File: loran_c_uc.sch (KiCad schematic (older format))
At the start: 33 parts, among them U1 STM32F407VG

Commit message: Almost done: SPI, Relay optocouplers, ADC & DAC interface However, bug needs to be fixed: buses are not connected between hierarchical sheets
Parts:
- removed C7, C8: 2.2u 6.3v, symbol CP1
- removed D? (x2): SMLVT3V3, symbol ZENER
- added C701: 10n, symbol C
- added C712, C713: 2.2u 10V CER, symbol C
- added D701: BAS85, symbol DIODESCH
- added JP702: RESET, symbol JUMPER
- added R709, R710: 33, symbol R
- C704, C705: renamed from C?; value 2.2u TAN -> 10u 6.3V Ta
- C711: renamed from C6; value 4.7u 6.3v -> 10u 6.3V Ta
- gave numbers to parts that had none: 20
- renumbered C1 to C706, C2 to C707, C3 to C708, C4 to C709, C5 to C710, U1 to U701
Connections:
- net labels added: BPROG, BREL, BSWD, NTRST, REL1, REL2, REL3, REL4, RELAY, SPI_STRB, SWCLK, SWD, SWDIO
- net labels removed: BJTAG, BPROGOUT, JTAG_SWD, JTAG_TCK_SWCLK, JTAG_TDI, JTAG_TMS_SWDIO, SPI_RD, SPI_WR
- wire segments 139 -> 125
- no-connect marks 0 -> 35
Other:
- moved on the sheet: JP701, R704

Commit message: FIXED: no more buses on hierarchical sheet ports
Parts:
- added R715: 33, symbol R
- FB701: value BEAD -> Bead
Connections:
- net SWDIO: now also R715.1; no longer U701.72 (PA13/JTMS/SWDIO/EVENTOUT)
- net NTRST renamed SWNTRST
- net REL1 renamed RELAY1
- net REL2 renamed RELAY2
- net REL3 renamed RELAY3
- net REL4 renamed RELAY4
- new net: R715.2, U701.72 (PA13/JTMS/SWDIO/EVENTOUT)
- no-connect marks 35 -> 39
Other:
- moved on the sheet: C714, C715, D701, X701

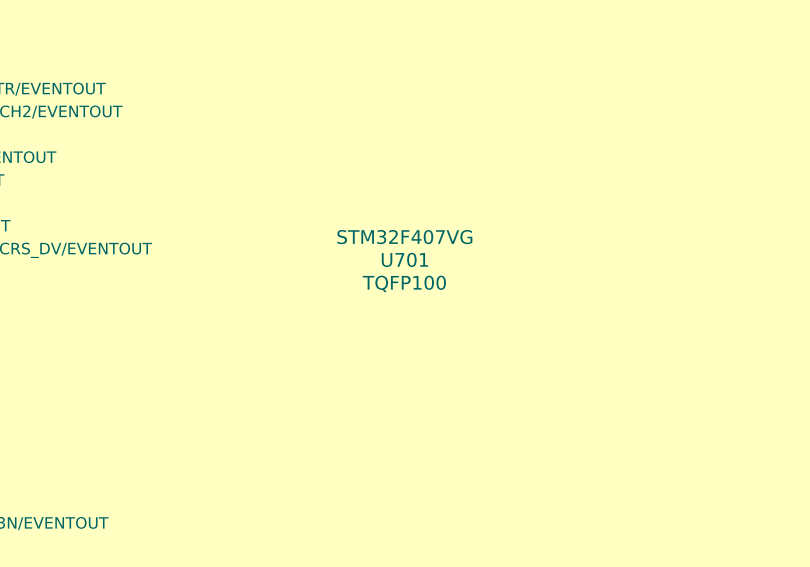
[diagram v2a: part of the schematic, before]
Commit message: Update: fix, assign modules to components -Fix P302 incorrect connection -Assign footprints to components (not all yet) -Back-import footprints into schematic fields
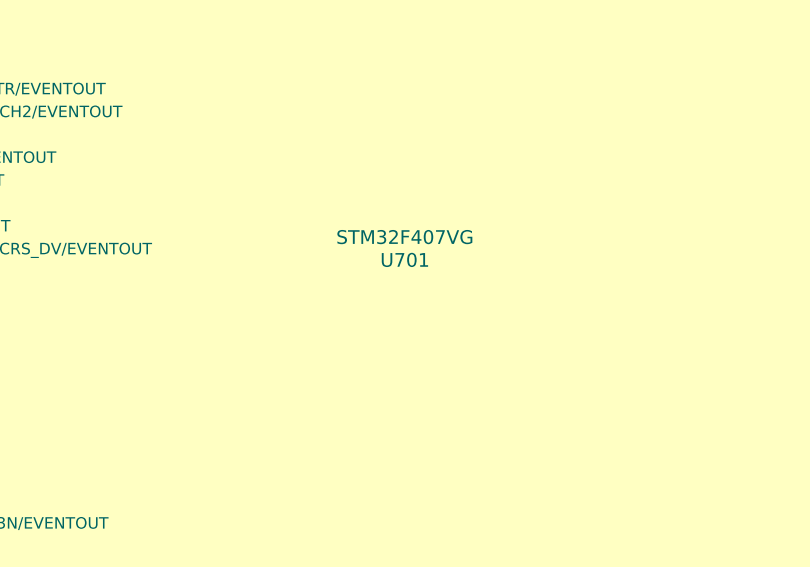
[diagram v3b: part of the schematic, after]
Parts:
- C701, C702, C703, C706, C707, C708, C709, C710, C712, C713, C714, C715: footprint (none) -> w_smd_capacitors:c_1206
- C704, C705, C711: footprint (none) -> w_smd_capacitors:c_tant_B
- D701, D702: footprint (none) -> w_smd_diode:sod80c
- FB701: footprint (none) -> w_pth_resistors:RC07
- JP701, JP702: footprint (none) -> Pin_Headers:Pin_Header_Straight_1x02
- R701, R702, R703, R704, R705, R706, R707, R708, R709, R710, R711, R712, R713, R714, R715: footprint (none) -> w_smd_resistors:r_1206
- U701: footprint TQFP100 -> w_smd_lqfp:TQFP-100
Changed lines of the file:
@@
 Date "15 янв. 2014"
 Rev "1"
-Comp "Roman Dobrodiy"
+Comp "Roman Dobrodiy (aka RomaVis)"
 Comment1 ""
 Comment2 ""
@@
 F 0 "U701" H 8350 5250 60  0000 C CNN
 F 1 "STM32F407VG" H 8350 5350 60  0000 C CNN
-F 2 "TQFP100" H 8350 5150 60  0000 C CNN
+F 2 "w_smd_lqfp:TQFP-100" H 8350 5150 60  0001 C CNN
 F 3 "" H 8350 5250 60  0000 C CNN
 	1    8350 5250
@@
 F 0 "C706" H 7600 1500 40  0000 L CNN
 F 1 "100n" H 7606 1315 40  0000 L CNN
-F 2 "" H 7638 1250 30  0000 C CNN
+F 2 "w_smd_capacitors:c_1206" H 7638 1250 30  0001 C CNN
 F 3 "" H 7600 1400 60  0000 C CNN
 	1    7600 1400
@@
 F 0 "C707" H 7900 1500 40  0000 L CNN
 F 1 "100n" H 7906 1315 40  0000 L CNN
-F 2 "" H 7938 1250 30  0000 C CNN
+F 2 "w_smd_capacitors:c_1206" H 7938 1250 30  0001 C CNN
 F 3 "" H 7900 1400 60  0000 C CNN
 	1    7900 1400
@@
 F 0 "C708" H 8200 1500 40  0000 L CNN
 F 1 "100n" H 8206 1315 40  0000 L CNN
-F 2 "" H 8238 1250 30  0000 C CNN
+F 2 "w_smd_capacitors:c_1206" H 8238 1250 30  0001 C CNN
 F 3 "" H 8200 1400 60  0000 C CNN
 	1    8200 1400
@@
 F 0 "C709" H 8500 1500 40  0000 L CNN
 F 1 "100n" H 8506 1315 40  0000 L CNN
-F 2 "" H 8538 1250 30  0000 C CNN
+F 2 "w_smd_capacitors:c_1206" H 8538 1250 30  0001 C CNN
 F 3 "" H 8500 1400 60  0000 C CNN
 	1    8500 1400
@@
 F 0 "C710" H 8800 1500 40  0000 L CNN
 F 1 "100n" H 8806 1315 40  0000 L CNN
-F 2 "" H 8838 1250 30  0000 C CNN
+F 2 "w_smd_capacitors:c_1206" H 8838 1250 30  0001 C CNN
 F 3 "" H 8800 1400 60  0000 C CNN
 	1    8800 1400
@@
 F 0 "C711" H 9150 1500 50  0000 L CNN
 F 1 "10u 6.3V Ta" H 9100 1300 50  0000 L CNN
-F 2 "" H 9100 1400 60  0000 C CNN
+F 2 "w_smd_capacitors:c_tant_B" H 9100 1400 60  0001 C CNN
 F 3 "" H 9100 1400 60  0000 C CNN
 	1    9100 1400
@@
 F 0 "R713" V 6180 1450 40  0000 C CNN
 F 1 "100" V 6107 1451 40  0000 C CNN
-F 2 "" V 6030 1450 30  0000 C CNN
+F 2 "w_smd_resistors:r_1206" V 6030 1450 30  0001 C CNN
 F 3 "" H 6100 1450 30  0000 C CNN
 	1    6100 1450
@@
 F 0 "C705" H 5450 2100 50  0000 L CNN
 F 1 "10u 6.3V Ta" H 5450 1900 50  0000 L CNN
-F 2 "" H 5400 2000 60  0000 C CNN
+F 2 "w_smd_capacitors:c_tant_B" H 5400 2000 60  0001 C CNN
 F 3 "" H 5400 2000 60  0000 C CNN
 	1    5400 2000
@@
 F 0 "C703" H 5000 2100 40  0000 L CNN
 F 1 "100n" H 5006 1915 40  0000 L CNN
-F 2 "" H 5038 1850 30  0000 C CNN
+F 2 "w_smd_capacitors:c_1206" H 5038 1850 30  0001 C CNN
 F 3 "" H 5000 2000 60  0000 C CNN
 	1    5000 2000
@@
 F 0 "C704" H 5450 1450 50  0000 L CNN
 F 1 "10u 6.3V Ta" H 5450 1250 50  0000 L CNN
-F 2 "" H 5400 1350 60  0000 C CNN
+F 2 "w_smd_capacitors:c_tant_B" H 5400 1350 60  0001 C CNN
 F 3 "" H 5400 1350 60  0000 C CNN
 	1    5400 1350
@@
 F 0 "C702" H 5000 1450 40  0000 L CNN
 F 1 "100n" H 5006 1265 40  0000 L CNN
-F 2 "" H 5038 1200 30  0000 C CNN
+F 2 "w_smd_capacitors:c_1206" H 5038 1200 30  0001 C CNN
 F 3 "" H 5000 1350 60  0000 C CNN
 	1    5000 1350
@@
 F 0 "JP701" H 1650 1600 60  0000 C CNN
 F 1 "BOOT_SEL" H 1650 1370 40  0000 C CNN
-F 2 "" H 1650 1450 60  0000 C CNN
+F 2 "Pin_Headers:Pin_Header_Straight_1x02" H 1650 1450 60  0001 C CNN
 F 3 "" H 1650 1450 60  0000 C CNN
 	1    1650 1450
@@
 F 0 "R704" V 2130 1750 40  0000 C CNN
 F 1 "3.3k" V 2057 1751 40  0000 C CNN
-F 2 "" V 1980 1750 30  0000 C CNN
+F 2 "w_smd_resistors:r_1206" V 1980 1750 30  0001 C CNN
 F 3 "" H 2050 1750 30  0000 C CNN
 	1    2050 1750
@@
 F 0 "R703" V 2080 6500 40  0000 C CNN
 F 1 "3.3k" V 2007 6501 40  0000 C CNN
-F 2 "" V 1930 6500 30  0000 C CNN
+F 2 "w_smd_resistors:r_1206" V 1930 6500 30  0001 C CNN
 F 3 "" H 2000 6500 30  0000 C CNN
 	1    2000 6500
@@
 F 0 "X701" H 14850 8150 60  0000 C CNN
 F 1 "32.768KHz" H 14850 7850 60  0000 C CNN
-F 2 "" H 14850 8000 60  0000 C CNN
+F 2 "" H 14850 8000 60  0001 C CNN
 F 3 "" H 14850 8000 60  0000 C CNN
 	1    14850 8000
@@
 F 0 "C714" H 15350 7800 40  0000 L CNN
 F 1 "15p" H 15356 7615 40  0000 L CNN
-F 2 "" H 15388 7550 30  0000 C CNN
+F 2 "w_smd_capacitors:c_1206" H 15388 7550 30  0001 C CNN
 F 3 "" H 15350 7700 60  0000 C CNN
 	1    15350 7700
@@
 F 0 "C715" H 15350 8400 40  0000 L CNN
 F 1 "15p" H 15356 8215 40  0000 L CNN
-F 2 "" H 15388 8150 30  0000 C CNN
+F 2 "w_smd_capacitors:c_1206" H 15388 8150 30  0001 C CNN
 F 3 "" H 15350 8300 60  0000 C CNN
 	1    15350 8300
@@
 F 0 "R711" V 3080 8150 40  0000 C CNN
 F 1 "3.3k" V 3007 8151 40  0000 C CNN
-F 2 "" V 2930 8150 30  0000 C CNN
+F 2 "w_smd_resistors:r_1206" V 2930 8150 30  0001 C CNN
 F 3 "" H 3000 8150 30  0000 C CNN
 	1    3000 8150
@@
 F 0 "R712" V 3330 8150 40  0000 C CNN
 F 1 "3.3k" V 3257 8151 40  0000 C CNN
-F 2 "" V 3180 8150 30  0000 C CNN
+F 2 "w_smd_resistors:r_1206" V 3180 8150 30  0001 C CNN
 F 3 "" H 3250 8150 30  0000 C CNN
 	1    3250 8150
@@
 F 0 "R702" V 2080 6300 40  0000 C CNN
 F 1 "3.3k" V 2007 6301 40  0000 C CNN
-F 2 "" V 1930 6300 30  0000 C CNN
+F 2 "w_smd_resistors:r_1206" V 1930 6300 30  0001 C CNN
 F 3 "" H 2000 6300 30  0000 C CNN
 	1    2000 6300
@@
 F 0 "R701" V 2080 6100 40  0000 C CNN
 F 1 "3.3k" V 2007 6101 40  0000 C CNN
-F 2 "" V 1930 6100 30  0000 C CNN
+F 2 "w_smd_resistors:r_1206" V 1930 6100 30  0001 C CNN
 F 3 "" H 2000 6100 30  0000 C CNN
 	1    2000 6100
@@
 F 0 "D702" H 6900 1000 40  0000 C CNN
 F 1 "BAS85" H 6900 800 40  0000 C CNN
-F 2 "" H 6900 900 60  0000 C CNN
+F 2 "w_smd_diode:sod80c" H 6900 900 60  0001 C CNN
 F 3 "" H 6900 900 60  0000 C CNN
 	1    6900 900
@@
 F 0 "FB701" H 7550 1050 60  0000 C CNN
 F 1 "Bead" H 7550 800 60  0000 C CNN
-F 2 "" H 7550 900 60  0000 C CNN
+F 2 "w_pth_resistors:RC07" H 7550 900 60  0001 C CNN
 F 3 "" H 7550 900 60  0000 C CNN
 	1    7550 900
@@
 F 0 "R706" V 2200 7200 40  0000 C CNN
 F 1 "33" V 2157 7401 40  0000 C CNN
-F 2 "" V 2080 7400 30  0000 C CNN
+F 2 "w_smd_resistors:r_1206" V 2080 7400 30  0001 C CNN
 F 3 "" H 2150 7400 30  0000 C CNN
 	1    2150 7400
@@
 F 0 "R707" V 2200 7300 40  0000 C CNN
 F 1 "33" V 2157 7501 40  0000 C CNN
-F 2 "" V 2080 7500 30  0000 C CNN
+F 2 "w_smd_resistors:r_1206" V 2080 7500 30  0001 C CNN
 F 3 "" H 2150 7500 30  0000 C CNN
 	1    2150 7500
@@
 F 0 "R708" V 2200 7400 40  0000 C CNN
 F 1 "33" V 2157 7601 40  0000 C CNN
-F 2 "" V 2080 7600 30  0000 C CNN
+F 2 "w_smd_resistors:r_1206" V 2080 7600 30  0001 C CNN
 F 3 "" H 2150 7600 30  0000 C CNN
 	1    2150 7600
@@
 F 0 "R705" V 2200 4500 40  0000 C CNN
 F 1 "33" V 2157 4701 40  0000 C CNN
-F 2 "" V 2080 4700 30  0000 C CNN
+F 2 "w_smd_resistors:r_1206" V 2080 4700 30  0001 C CNN
 F 3 "" H 2150 4700 30  0000 C CNN
 	1    2150 4700
@@
 F 0 "R714" V 13800 6200 40  0000 C CNN
 F 1 "33" V 13757 6401 40  0000 C CNN
-F 2 "" V 13680 6400 30  0000 C CNN
+F 2 "w_smd_resistors:r_1206" V 13680 6400 30  0001 C CNN
 F 3 "" H 13750 6400 30  0000 C CNN
 	1    13750 6400
@@
 F 0 "C701" H 2050 2600 40  0000 L CNN
 F 1 "10n" H 2056 2415 40  0000 L CNN
-F 2 "" H 2088 2350 30  0000 C CNN
+F 2 "w_smd_capacitors:c_1206" H 2088 2350 30  0001 C CNN
 F 3 "" H 2050 2500 60  0000 C CNN
 	1    2050 2500
@@
 F 0 "JP702" H 1650 2400 60  0000 C CNN
 F 1 "RESET" H 1650 2170 40  0000 C CNN
-F 2 "" H 1650 2250 60  0000 C CNN
+F 2 "Pin_Headers:Pin_Header_Straight_1x02" H 1650 2250 60  0001 C CNN
 F 3 "" H 1650 2250 60  0000 C CNN
 	1    1650 2250
@@
 F 0 "D701" H 2800 3600 40  0000 C CNN
 F 1 "BAS85" H 2800 3400 40  0000 C CNN
-F 2 "" H 2800 3500 60  0000 C CNN
+F 2 "w_smd_diode:sod80c" H 2800 3500 60  0001 C CNN
 F 3 "" H 2800 3500 60  0000 C CNN
 	1    2800 3500
@@
 F 0 "C712" H 9250 8750 40  0000 L CNN
 F 1 "2.2u 10V CER" H 9256 8565 40  0000 L CNN
-F 2 "" H 9288 8500 30  0000 C CNN
+F 2 "w_smd_capacitors:c_1206" H 9288 8500 30  0001 C CNN
 F 3 "" H 9250 8650 60  0000 C CNN
 	1    9250 8650
@@
 F 0 "C713" H 9750 8750 40  0000 L CNN
 F 1 "2.2u 10V CER" H 9756 8565 40  0000 L CNN
-F 2 "" H 9788 8500 30  0000 C CNN
+F 2 "w_smd_capacitors:c_1206" H 9788 8500 30  0001 C CNN
 F 3 "" H 9750 8650 60  0000 C CNN
 	1    9750 8650
@@
 F 0 "R709" V 2900 6900 40  0000 C CNN
 F 1 "33" V 2857 7101 40  0000 C CNN
-F 2 "" V 2780 7100 30  0000 C CNN
+F 2 "w_smd_resistors:r_1206" V 2780 7100 30  0001 C CNN
 F 3 "" H 2850 7100 30  0000 C CNN
 	1    2850 7100
@@
 F 0 "R710" V 2900 7000 40  0000 C CNN
 F 1 "33" V 2857 7201 40  0000 C CNN
-F 2 "" V 2780 7200 30  0000 C CNN
+F 2 "w_smd_resistors:r_1206" V 2780 7200 30  0001 C CNN
 F 3 "" H 2850 7200 30  0000 C CNN
 	1    2850 7200
@@
 F 0 "R715" V 2200 4000 40  0000 C CNN
 F 1 "33" V 2157 4201 40  0000 C CNN
-F 2 "" V 2080 4200 30  0000 C CNN
+F 2 "w_smd_resistors:r_1206" V 2080 4200 30  0001 C CNN
 F 3 "" H 2150 4200 30  0000 C CNN
 	1    2150 4200
